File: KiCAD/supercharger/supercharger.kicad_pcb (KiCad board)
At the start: 2 copper layers, 49.7 x 10 mm, 24 parts, among them J2 BAT, J4 UJC-H-G-SMT-1-P6-TR

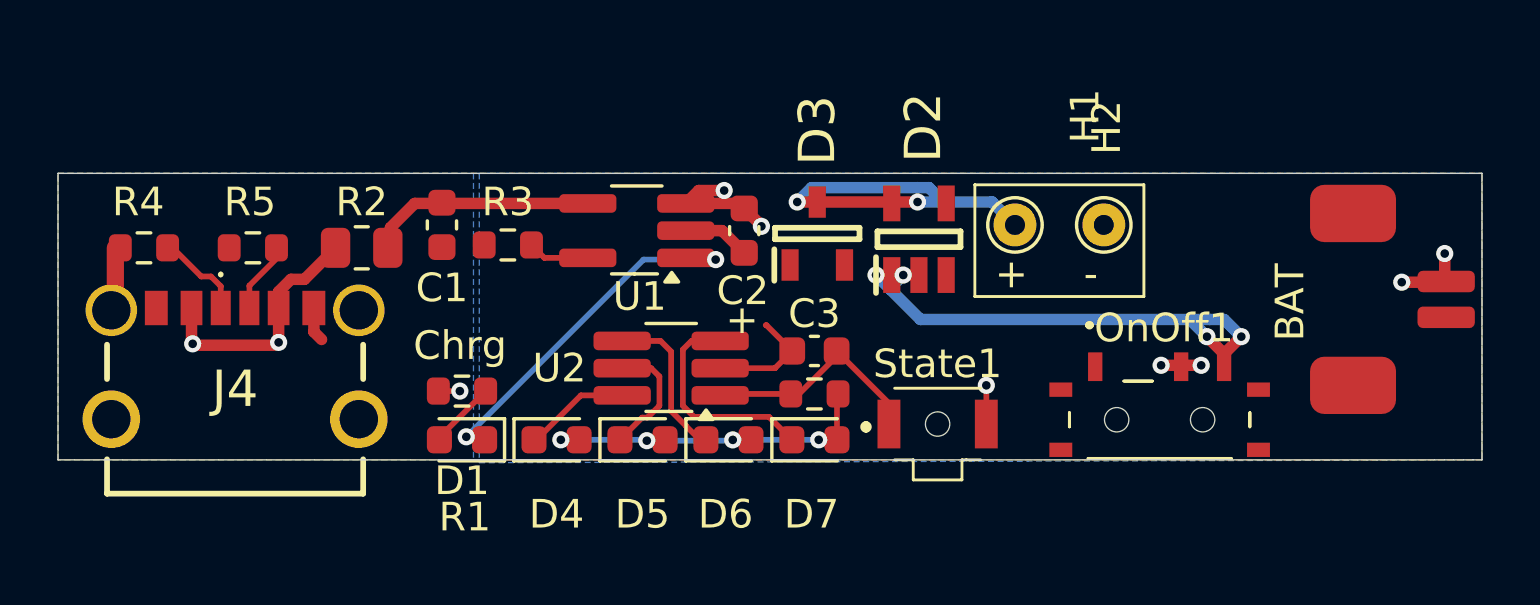
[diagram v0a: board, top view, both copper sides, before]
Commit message: PCB: Massive blunder around D2 fixed.
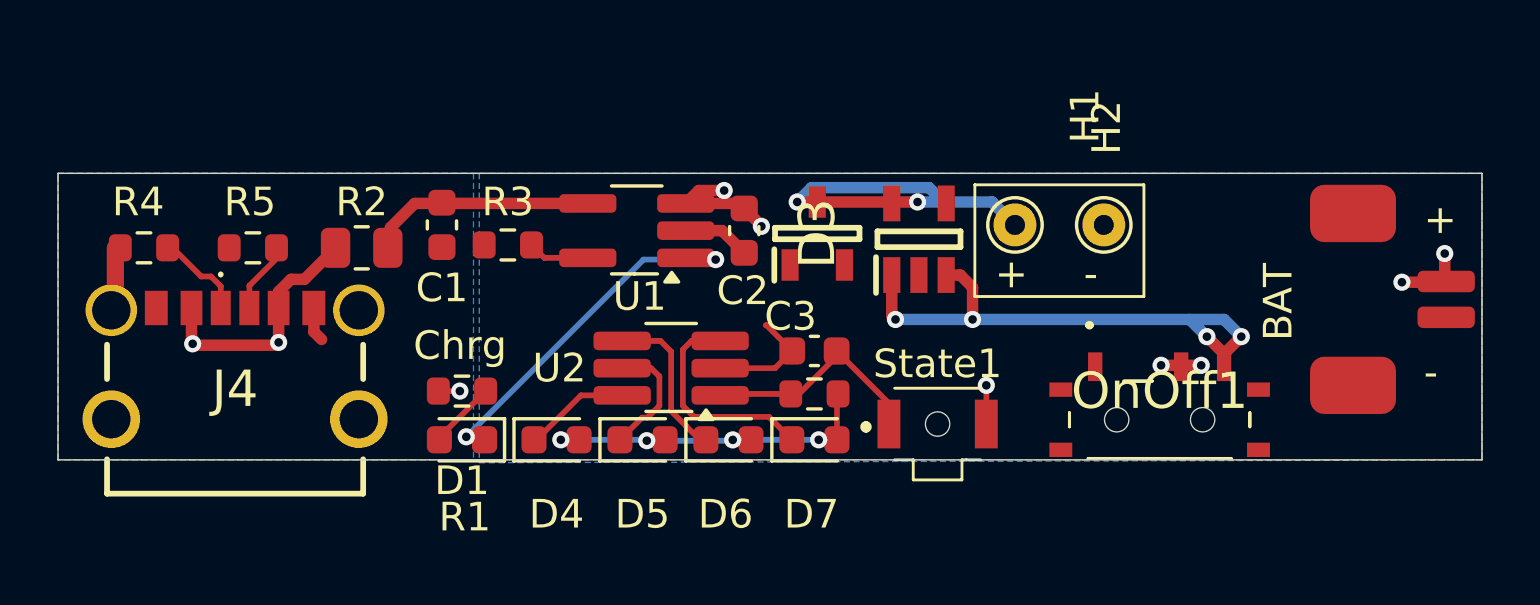
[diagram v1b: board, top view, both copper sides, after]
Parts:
- R2: value 0R5 -> 0R
- U1: value ~ -> STC4054
- U2: value ~ -> HM1160
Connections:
- D2 pad 1: Net-(D2-GND) -> Net-(D2-EN)
- D2 pad 2: Net-(D2-GND) -> GND
- D2 pad 3: GND -> Net-(D2-EN)
- OnOff1 pad C1: Net-(D2-GND) -> Net-(D2-EN)
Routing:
- net Net-(D2-GND): track 19.3 -> 0.00 mm, vias 4 -> 0
- net Net-(D2-EN): track 0.00 -> 19.1 mm, vias 0 -> 4

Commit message: Round-off tracks
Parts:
- D2: footprint EC-parts:SOT95P280X145-5N -> Package_TO_SOT_SMD:SOT-23-5_HandSoldering
- D3: footprint EC-parts:SOT95P248X115-3N -> Package_TO_SOT_SMD:SOT-23-3
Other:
- board text added: "Supercharger v1.1"
- board text removed: "Supercharger v1.0"

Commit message: Board made 0.8mm higher. Little component placement tweaks.
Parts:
- moved H2 0.81 mm to (126.4, 91.0)
- moved H1 0.80 mm to (123.4, 91.0)
- moved R2 0.80 mm to (100.6, 91.8)
- moved R5 0.63 mm to (96.6, 92.0)
- moved R4 0.60 mm to (93.0, 92.0)
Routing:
- net GND: track 9.56 -> 7.52 mm
- net Net-(J4-CC2): track 2.32 -> 2.95 mm
- net +5V: track 9.20 -> 9.81 mm
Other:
- board size 49.7 x 10 mm -> 49.7 x 10.8 mm
- board text added: "Supercharger v1.2"
- board text removed: "Supercharger v1.1"
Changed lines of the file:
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@@
 		(tags "resistor")
 		(property "Reference" "R3"
-			(at 0 1.5 0)
+			(at 0.1 1.3 0)
 			(layer "F.SilkS")
 			(effects
@@
 	(footprint "Resistor_SMD:R_0603_1608Metric"
 		(layer "F.Cu")
-		(at 96.8 92.6 180)
+		(at 96.6 92 180)
 		(descr "Resistor SMD 0603 (1608 Metric), square (rectangular) end terminal, IPC_7351 nominal, (Body size source: IPC-SM-782 page 72, https://www.pcb-3d.com/wordpress/wp-content/uploads/ipc-sm-782a_amendment_1_and_2.pdf), generated with kicad-footprint-generator")
 		(tags "resistor")
 		(property "Reference" "R5"
-			(at 0.1 1.6 180)
+			(at 0 1.8 180)
 			(layer "F.SilkS")
 			(effects
@@
 	(footprint "Resistor_SMD:R_0805_2012Metric"
 		(layer "F.Cu")
-		(at 100.6 92.6)
+		(at 100.6 91.8)
 		(descr "Resistor SMD 0805 (2012 Metric), square (rectangular) end terminal, IPC_7351 nominal, (Body size source: IPC-SM-782 page 72, https://www.pcb-3d.com/wordpress/wp-content/uploads/ipc-sm-782a_amendment_1_and_2.pdf), generated with kicad-footprint-generator")
 		(tags "resistor")
@@
 	(footprint "TestPoint:TestPoint_THTPad_D1.5mm_Drill0.7mm"
 		(layer "F.Cu")
-		(at 123.4 91.8 -90)
+		(at 123.4 91 -90)
 		(descr "THT pad as test Point, diameter 1.5mm, hole diameter 0.7mm")
 		(tags "test point THT pad")
@@
 	(footprint "Resistor_SMD:R_0603_1608Metric"
 		(layer "F.Cu")
-		(at 93 92.6 180)
+		(at 93 92 180)
 		(descr "Resistor SMD 0603 (1608 Metric), square (rectangular) end terminal, IPC_7351 nominal, (Body size source: IPC-SM-782 page 72, https://www.pcb-3d.com/wordpress/wp-content/uploads/ipc-sm-782a_amendment_1_and_2.pdf), generated with kicad-footprint-generator")
 		(tags "resistor")
 		(property "Reference" "R4"
-			(at 0.2 1.6 180)
+			(at 0 1.8 180)
 			(layer "F.SilkS")
 			(effects
@@
 	(footprint "TestPoint:TestPoint_THTPad_D1.5mm_Drill0.7mm"
 		(layer "F.Cu")
-		(at 126.5 91.8 -90)
+		(at 126.4 91 -90)
 		(descr "THT pad as test Point, diameter 1.5mm, hole diameter 0.7mm")
 		(tags "test point THT pad")
@@
 	)
 	(gr_rect
-		(start 122 90.4)
-		(end 127.9 94.3)
+		(start 122 89.45)
+		(end 127.9 93.35)
 		(stroke
 			(width 0.1)
@@
 	)
 	(gr_rect
-		(start 90 90)
+		(start 90 89.2)
 		(end 139.7 100)
 		(stroke
@@
 		(layer "Edge.Cuts")
 	)
-	(gr_text "Supercharger\nv1.1"
+	(gr_text "Supercharger\nv1.2"
 		(at 138.8 93.9 0)
 		(layer "B.SilkS")
@@
 	)
 	(gr_text "-"
-		(at 125.8 94.1 0)
+		(at 125.8 93.2 0)
 		(layer "F.SilkS")
 		(effects
@@
 	)
 	(gr_text "+"
-		(at 122.7 94.1 0)
+		(at 122.7 93.2 0)
 		(layer "F.SilkS")
 		(effects
@@
 		(layer "User.1")
 		(pts
-			(xy 139.7 90) (xy 126.5 90)
+			(xy 139.7 89.2) (xy 126.5 89.2)
 		)
 		(height 10.4)
 		(gr_text "13.2000 mm"
-			(at 133.1 78.45 0)
+			(at 133.1 77.65 0)
 			(layer "User.1")
 			(effects
@@
 		(layer "User.1")
 		(pts
-			(xy 139.8 89.7) (xy 90.1 89.7)
+			(xy 139.7 89.2) (xy 90 89.2)
 		)
 		(height 3.899999)
 		(gr_text "49.7000 mm"
-			(at 114.95 84.000001 0)
+			(at 114.85 83.500001 0)
 			(layer "User.1")
 			(effects
@@
 		(layer "User.1")
 		(pts
-			(xy 139.7 90) (xy 123.4 90)
+			(xy 139.7 89.2) (xy 123.4 89.2)
 		)
 		(height 13.8)
 		(gr_text "16.3000 mm"
-			(at 131.55 75.05 0)
+			(at 131.55 74.25 0)
 			(layer "User.1")
 			(effects
@@
 		(layer "User.1")
 		(pts
-			(xy 139.7 90) (xy 139.7 100)
+			(xy 139.7 89.2) (xy 139.7 100)
 		)
 		(height -5.2)
-		(gr_text "10.0000 mm"
+		(gr_text "10.8000 mm"
 			(at 147.2 94.6 90)
 			(layer "User.1")
@@
 	)
 	(segment
-		(start 92 94.64)
-		(end 92 92.6)
-		(width 0.6)
-		(layer "F.Cu")
-		(net 1)
-	)
-	(segment
 		(start 115.625 96.2)
 		(end 114.725 95.3)
@@
 	)
 	(segment
-		(start 101.6 92.25)
-		(end 101.6 92.6)
-		(width 0.4)
-		(layer "F.Cu")
-		(net 2)
-	)
-	(segment
 		(start 103.05104 91.05)
 		(end 108.49 91.05)
@@
 	)
 	(segment
-		(start 94.7 95.95)
-		(end 94.66 95.91)
-		(width 0.4)
-		(layer "F.Cu")
-		(net 5)
-	)
-	(segment
-		(start 97.6 96)
-		(end 94.75 96)
+		(start 98.022617 93.464882)
+		(end 99.6875 91.8)
 		(width 0.4)
 		(layer "F.Cu")
@@
 	)
 	(segment
-		(start 98.6 93.7)
-		(end 99.6 92.7)
+		(start 97.7 94.24375)
+		(end 97.7 94.7)
 		(width 0.4)
 		(layer "F.Cu")
@@
 	)
 	(segment
-		(start 97.7 94.7)
-		(end 97.7 94.13)
+		(start 94.7 95.95)
+		(end 94.66 95.91)
 		(width 0.4)
 		(layer "F.Cu")
@@
 	)
 	(segment
-		(start 98.13 93.7)
-		(end 98.6 93.7)
+		(start 97.6 96)
+		(end 94.75 96)
 		(width 0.4)
 		(layer "F.Cu")
@@
 	)
 	(segment
-		(start 97.7 94.13)
-		(end 98.13 93.7)
-		(width 0.4)
-		(layer "F.Cu")
-		(net 5)
-	)
-	(segment
 		(start 94.66 95.91)
 		(end 94.66 94.7)
@@
 		(net 5)
 	)
+	(arc
+		(start 98.022617 93.464882)
+		(mid 97.783845 93.822229)
+		(end 97.7 94.24375)
+		(width 0.4)
+		(layer "F.Cu")
+		(net 5)
+	)
 	(segment
 		(start 106.975 92.95)
@@
 	)
 	(segment
-		(start 96.68 94.31)
-		(end 96.68 94.7)
+		(start 97.0525 92.3725)
+		(end 97.425 92)
 		(width 0.2)
 		(layer "F.Cu")
@@
 	)
 	(segment
-		(start 96.955771 93.644228)
-		(end 97.8 92.8)
+		(start 96.68 93.271794)
+		(end 96.68 94.7)
 		(width 0.2)
 		(layer "F.Cu")
@@
 	)
 	(arc
-		(start 96.955771 93.644228)
-		(mid 96.75167 93.949686)
-		(end 96.68 94.31)
+		(start 97.0525 92.3725)
+		(mid 96.776809 92.785099)
+		(end 96.68 93.271794)
 		(width 0.2)
 		(layer "F.Cu")
@@
 	)
 	(segment
-		(start 94.879791 93.479791)
-		(end 94 92.6)
+		(start 93.825 92.1125)
+		(end 93.825 92)
 		(width 0.2)
 		(layer "F.Cu")
@@
 	)
 	(segment
-		(start 95.460208 93.720208)
-		(end 95.51 93.77)
-		(width 0.2)
-		(layer "F.Cu")
-		(net 8)
-	)
-	(segment
-		(start 95.68 94.180416)
+		(start 95.68 94.39)
 		(end 95.68 94.7)
 		(width 0.2)
@@
 		(net 8)
 	)
-	(arc
-		(start 95.51 93.77)
-		(mid 95.635818 93.9583)
-		(end 95.68 94.180416)
+	(segment
+		(start 93.904549 92.304549)
+		(end 95.460796 93.860796)
 		(width 0.2)
 		(layer "F.Cu")
@@
 	)
 	(arc
-		(start 94.879791 93.479791)
-		(mid 95.01294 93.568758)
-		(end 95.17 93.6)
+		(start 93.825 92.1125)
+		(mid 93.845674 92.216436)
+		(end 93.904549 92.304549)
 		(width 0.2)
 		(layer "F.Cu")
@@
 	)
 	(arc
-		(start 95.460208 93.720208)
-		(mid 95.327059 93.631241)
-		(end 95.17 93.6)
+		(start 95.460796 93.860796)
+		(mid 95.62303 94.103597)
+		(end 95.68 94.39)
 		(width 0.2)
 		(layer "F.Cu")
@@
 	)
 	(segment
-		(start 122.034314 91)
-		(end 120.9 91)
+		(start 120.9 91)
+		(end 122.034314 91)
 		(width 0.4)
 		(layer "B.Cu")
@@
 	)
 	(segment
-		(start 120.2 90.5)
-		(end 119.8 90.5)
+		(start 122.034314 91)
+		(end 123.4 91)
 		(width 0.4)
 		(layer "B.Cu")
@@
 	)
 	(segment
-		(start 123 91.4)
-		(end 123.4 91.8)
+		(start 120.2 90.5)
+		(end 119.8 90.5)
 		(width 0.4)
 		(layer "B.Cu")
@@
 		(net 11)
 	)
-	(arc
-		(start 123 91.4)
-		(mid 122.556939 91.103956)
-		(end 122.034314 91)
-		(width 0.4)
-		(layer "B.Cu")
-		(net 11)
-	)
 	(segment
 		(start 108.1875 99.3)
@@
 		(polygon
 			(pts
-				(xy 90 90) (xy 139.7 90) (xy 139.7 100) (xy 90 100)
+				(xy 90 89.2) (xy 139.7 89.2) (xy 139.7 100) (xy 90 100)
 			)
 		)
@@
 		(polygon
 			(pts
-				(xy 139.7 90) (xy 104.7 90) (xy 104.7 100.1) (xy 139.7 100)
+				(xy 139.7 89.2) (xy 104.7 89.2) (xy 104.7 100.1) (xy 139.7 100)
 			)
 		)
@@
 		(polygon
 			(pts
-				(xy 90 90) (xy 104.5 90) (xy 104.5 100) (xy 90 100)
+				(xy 90 89.2) (xy 104.5 89.2) (xy 104.5 100) (xy 90 100)
 			)
 		)
